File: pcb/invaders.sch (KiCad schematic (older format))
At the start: 56 parts, among them J1 USB_B_Micro, J2 ISP, J3 Batt_In, SW1 Reset, SW10 SW_SPDT, SW2 D_Left, SW3 Trig_Left, SW4 D_Up, SW5 D_Down, SW6 D_Right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

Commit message: library fixes
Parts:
- OLED1: renamed from D1; symbol A-symbols:OLED_Panel_I2C-invaders -> A-symbols:OLED_Panel_1in3_I2C
- OLED2: renamed from D2; symbol A-symbols:OLED_Panel_SPI_I2C-invaders -> A-symbols:OLED_Panel_2in42_SPI_I2C
- OLED3: renamed from D8; symbol A-symbols:OLED_Panel_RGB_SPI -> A-symbols:OLED_Panel_1in5_RGB_SPI
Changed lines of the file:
@@
 $EndComp
 $Comp
-L A-symbols:OLED_Panel_I2C-invaders D1
+L A-symbols:OLED_Panel_1in3_I2C OLED1
 U 1 1 5B71DB68
 P 4400 5450
-F 0 "D1" H 4750 5600 50  0000 L CNN
-F 1 "OLED_1in3" H 4750 5500 50  0000 L CNN
+F 0 "OLED1" H 4150 5400 50  0000 L CNN
+F 1 "OLED_1in3" H 4150 5300 50  0000 L CNN
 F 2 "invaders:OLED_1in3_i2c" H 4350 5400 50  0001 C CNN
 F 3 "" H 4350 5400 50  0001 C CNN
@@
 Text Label 3600 3950 0    50   ~ 0
 ADC0
-Text Label 4800 4350 0    50   ~ 0
-Panel_RST
 Wire Wire Line
 	3350 4150 3600 4150
@@
 Audio_Out
 $Comp
-L A-symbols:OLED_Panel_SPI_I2C-invaders D2
+L A-symbols:OLED_Panel_2in42_SPI_I2C OLED2
 U 1 1 5B8AAD32
 P 6150 5650
-F 0 "D2" H 6650 5550 50  0000 L CNN
-F 1 "OLED_2in42" H 6650 5450 50  0000 L CNN
+F 0 "OLED2" H 6000 5700 50  0000 L CNN
+F 1 "OLED_2in42" H 6000 5600 50  0000 L CNN
 F 2 "invaders:OLED_2in42_spi_i2c" H 6150 5650 50  0001 C CNN
 F 3 "" H 6150 5650 50  0001 C CNN
@@
 	5550 5850 5300 5850
 Wire Wire Line
-	5550 5750 5300 5750
-Wire Wire Line
-	5550 5550 5300 5550
-Wire Wire Line
-	5550 5650 5300 5650
-Text Label 5300 5650 0    50   ~ 0
+	5550 5750 5000 5750
+Wire Wire Line
+	5550 5550 5000 5550
+Wire Wire Line
+	5550 5650 5000 5650
+Text Label 5000 5650 0    50   ~ 0
 Panel_DataCmd
-Text Label 5300 5750 0    50   ~ 0
+Text Label 5000 5750 0    50   ~ 0
 Panel_RST
-Text Label 5300 5550 0    50   ~ 0
+Text Label 5000 5550 0    50   ~ 0
 Panel_CS
 Wire Wire Line
@@
 Connection ~ 8950 3900
 $Comp
-L A-symbols:OLED_Panel_RGB_SPI D8
+L A-symbols:OLED_Panel_1in5_RGB_SPI OLED3
 U 1 1 5D403A31
 P 6150 6700
-F 0 "D8" H 6650 6600 50  0000 L CNN
-F 1 "OLED_1in5_RGB" H 6650 6500 50  0000 L CNN
+F 0 "OLED3" H 6000 6700 50  0000 L CNN
+F 1 "OLED_1in5_RGB" H 6000 6600 50  0000 L CNN
 F 2 "invaders:OLED_1in5_spi_rgb" H 6150 6700 50  0001 C CNN
 F 3 "" H 6150 6700 50  0001 C CNN

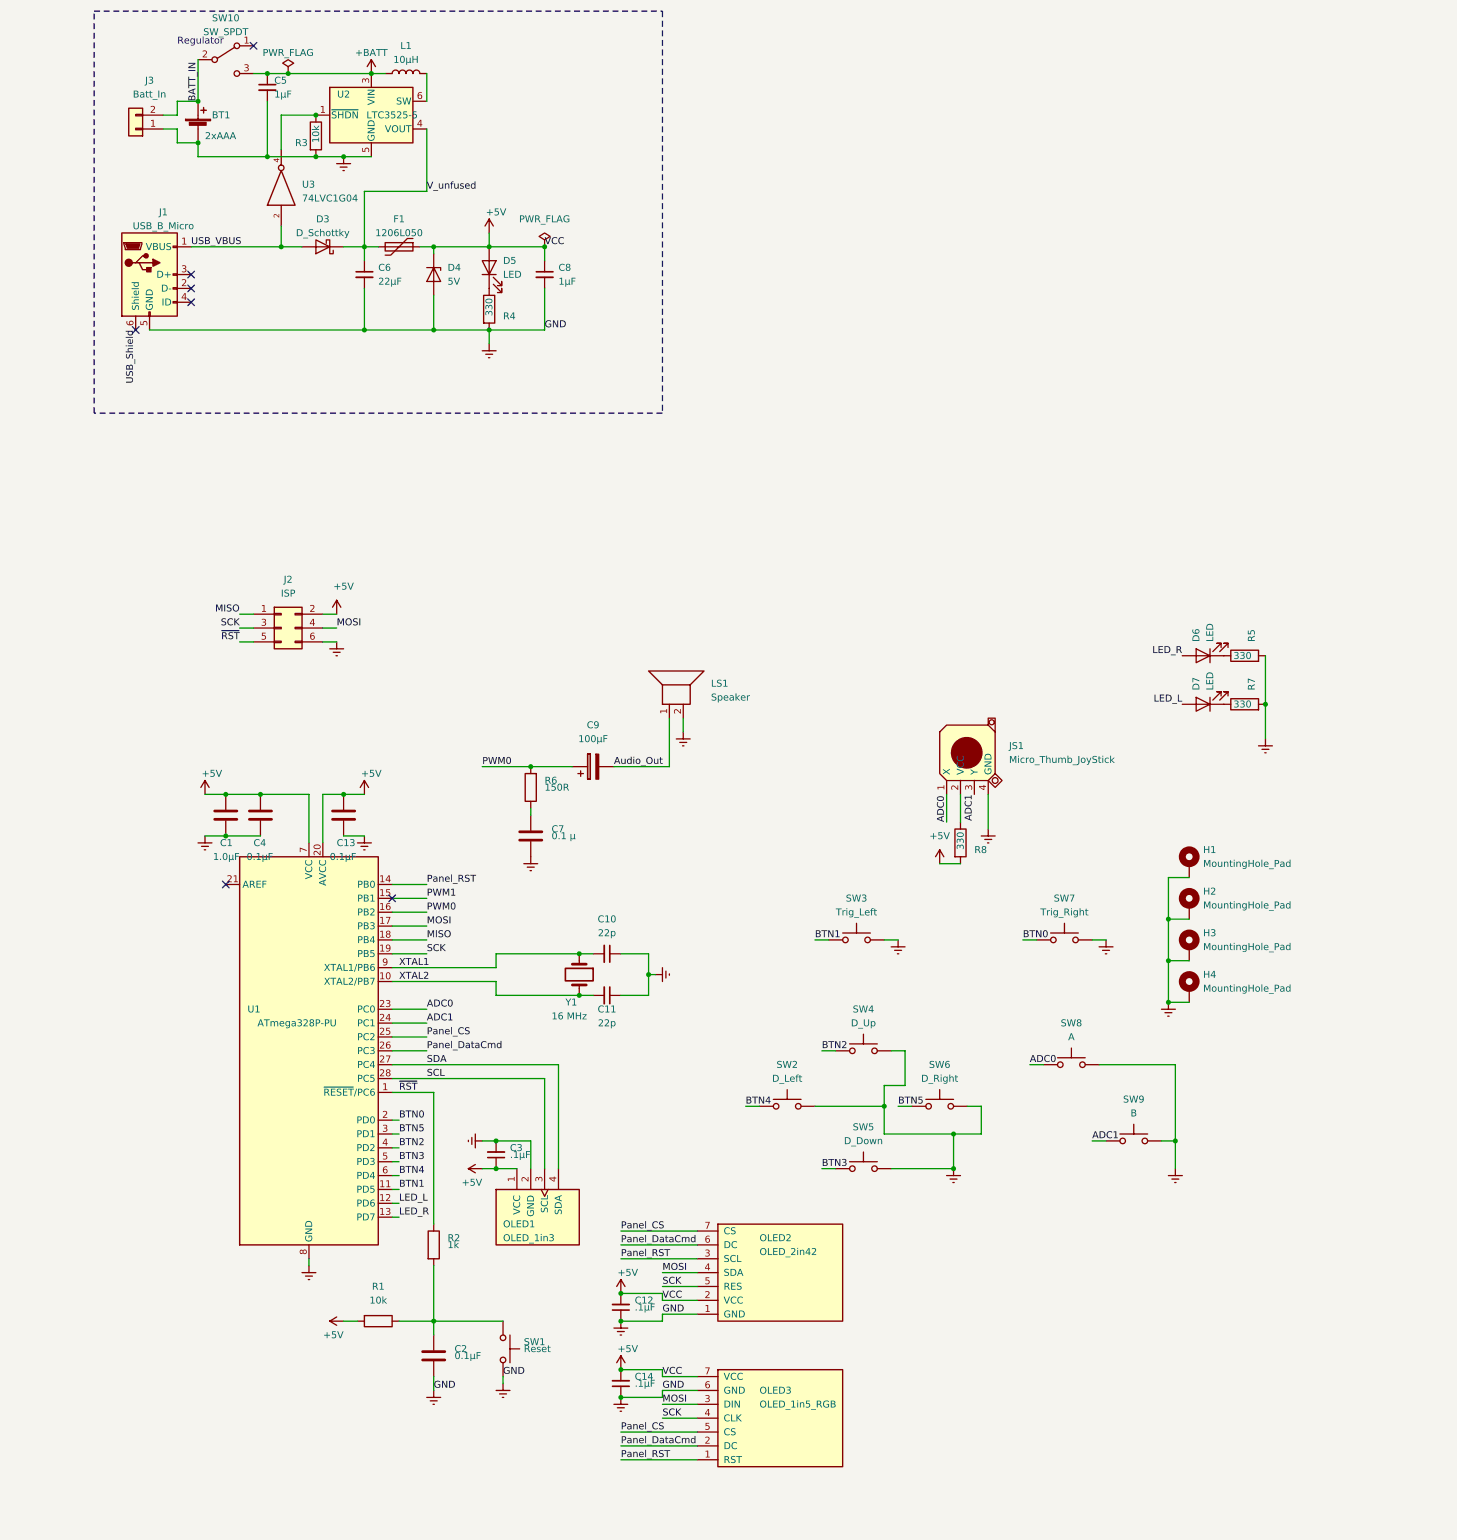
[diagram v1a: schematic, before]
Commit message: cleanup; add pullup to Panel_CS
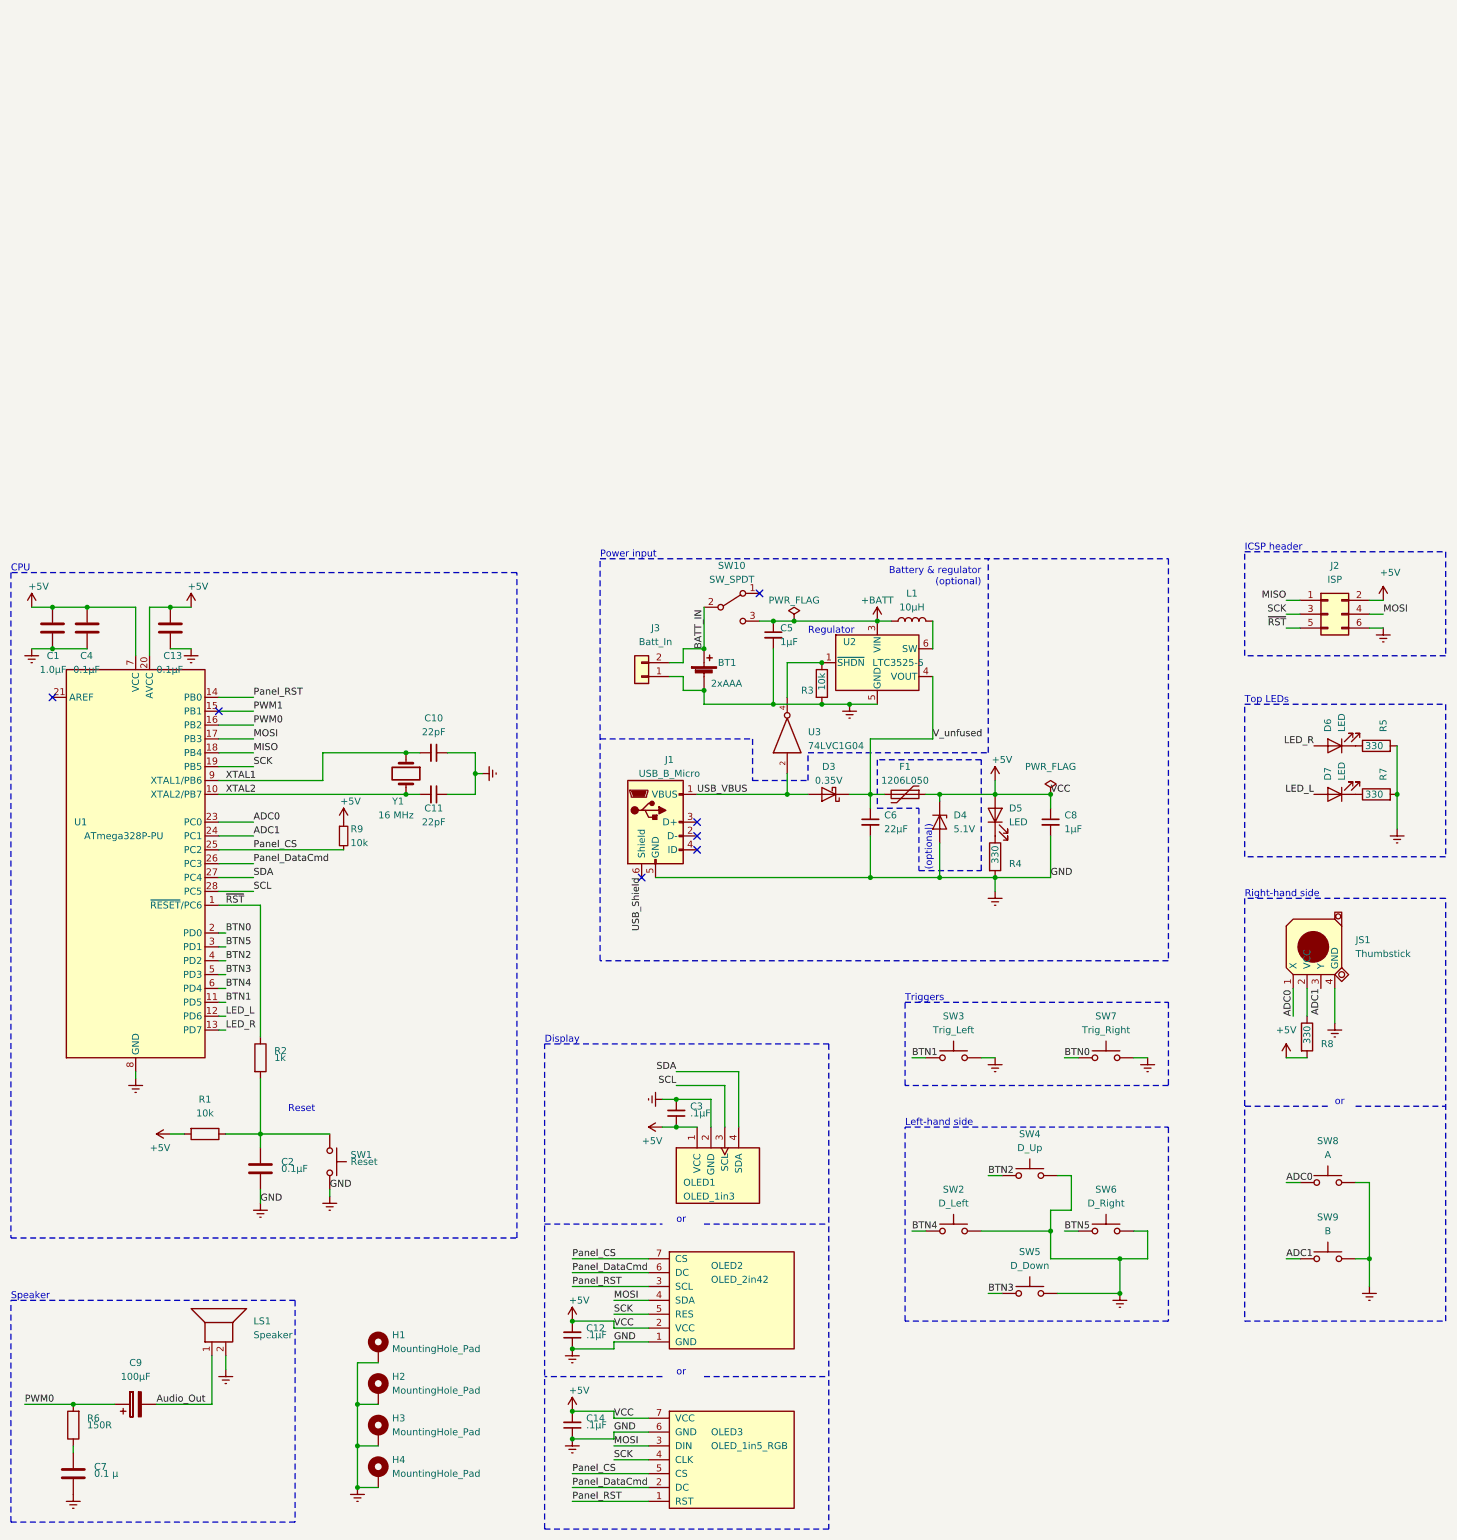
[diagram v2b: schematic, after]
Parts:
- added R9: 10k, Resistor_SMD:R_1206_3216Metric_Pad1.42x1.75mm_HandSolder, symbol Device:R_Small
- BT1: Part (none) -> Keystone 2468
- C10, C11: value 22p -> 22pF
- C6: Part (none) -> Taiyo LMK316ABJ226ML-T
- D3: value D_Schottky -> 0.35V; Part (none) -> Rohm RSX101MM-30TR
- D4: value 5V -> 5.1V; Part (none) -> RND 1N4733A
- J1: Part (none) -> Molex 105017
- JS1: value Micro_Thumb_JoyStick -> Thumbstick; footprint invaders:psp_thumbstick -> a-symbols:psp_thumbstick; Part (none) -> PSP1000 thumbstick
- OLED1: footprint invaders:OLED_1in3_i2c -> a-symbols:OLED_1in3_i2c
- OLED2: footprint invaders:OLED_2in42_spi_i2c -> a-symbols:OLED_2in42_spi_i2c
- OLED3: footprint invaders:OLED_1in5_spi_rgb -> a-symbols:OLED_1in5_spi_rgb
- SW1, SW2, SW4, SW5, SW6, SW8, SW9: Part (none) -> 6x6mm tactile, e.g. ALPS SKHHAMA010
- SW3, SW7: Part (none) -> 6mm angled tactile, e.g. C&K PTS645VM582LFS
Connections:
- net +5V: now also R9.1
- net Panel_CS: now also R9.2
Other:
- note added: "(optional)"
- note added: "Battery & regulator\n(optional)"
- note added: "CPU"
- note added: "Display"
- note added: "ICSP header"
- note added: "Left-hand side"
- note added: "Power input"
- note added: "Reset"
- note added: "Right-hand side"
- note added: "Speaker"
- note added: "Top LEDs"
- note added: "Triggers"
- note added: "or"
- moved on the sheet: BT1, C1, C10, C11, C12, C13, C14, C2, C3, C4, C5, C6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
